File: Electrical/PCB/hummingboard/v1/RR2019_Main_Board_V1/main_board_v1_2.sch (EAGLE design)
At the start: 147 parts, among them CN1 MIRCO_B, IC1 OR_SC70-5, J10 I2C_5V_4, J11 SERVO_LEFT, J12 SERVO_RIGHT, J13 ESC, J14 5V_INPUT, J15 QUAD_ENCODER_2, J16 7.2V_INPUT, J17 I2C_5V_FXIO_1, J18 I2C_5V_FXIO_2, J19 JETSON_TRIGGER, J2 REAR_ENCODER, J20 QUAD_ENCODER_1, J21 BLDC_HALL, J22 SPI_FXIO_1, J3 FRONT_ENCODER, J4 I2C_1V8_1, J5 SPI_2, J6 WIRELESS_MODULE, J7 UART_0, J8 UART_2, J9 STEERING_ANGLE, Q1 BSS138, Q3 DMP2066LSN, Q4 BSS138, Q5 BSS138, Q6 BSS138, Q7 BSS138, Q8 BSS138, U3 ICM-20948, U4 PCA9306

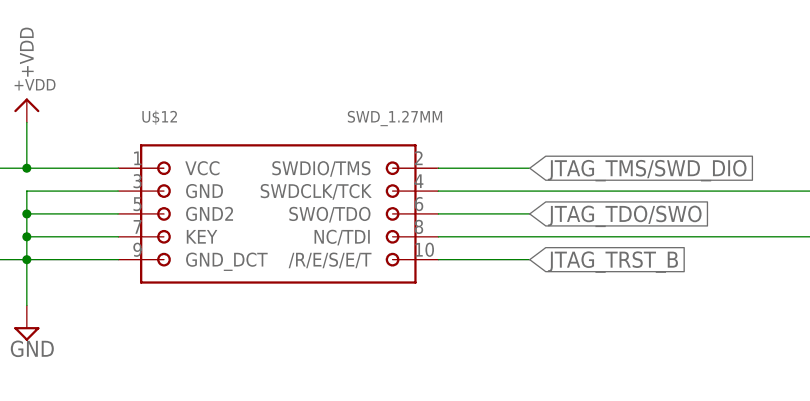
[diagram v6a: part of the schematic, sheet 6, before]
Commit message: silkscreen complete for board
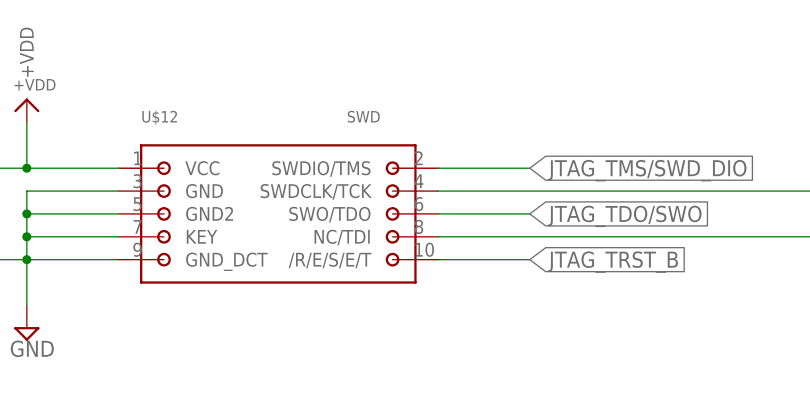
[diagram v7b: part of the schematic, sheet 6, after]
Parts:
- U$12: value SWD_1.27MM -> SWD
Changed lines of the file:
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@@
 <part name="R44" library="RobotRacing2019_Master" deviceset="RES0603" device="" value="10k"/>
 <part name="IC1" library="RobotRacing2019_Master" deviceset="OR_SC70-5" device=""/>
-<part name="U$12" library="RobotRacing2019_Master" deviceset="SWD_1.27MM" device=""/>
+<part name="U$12" library="RobotRacing2019_Master" deviceset="SWD_1.27MM" device="" value="SWD"/>
 <part name="U$18" library="RobotRacing2019_Master" deviceset="+5V" device=""/>
 <part name="U$20" library="RobotRacing2019_Master" deviceset="+3V3" device=""/>

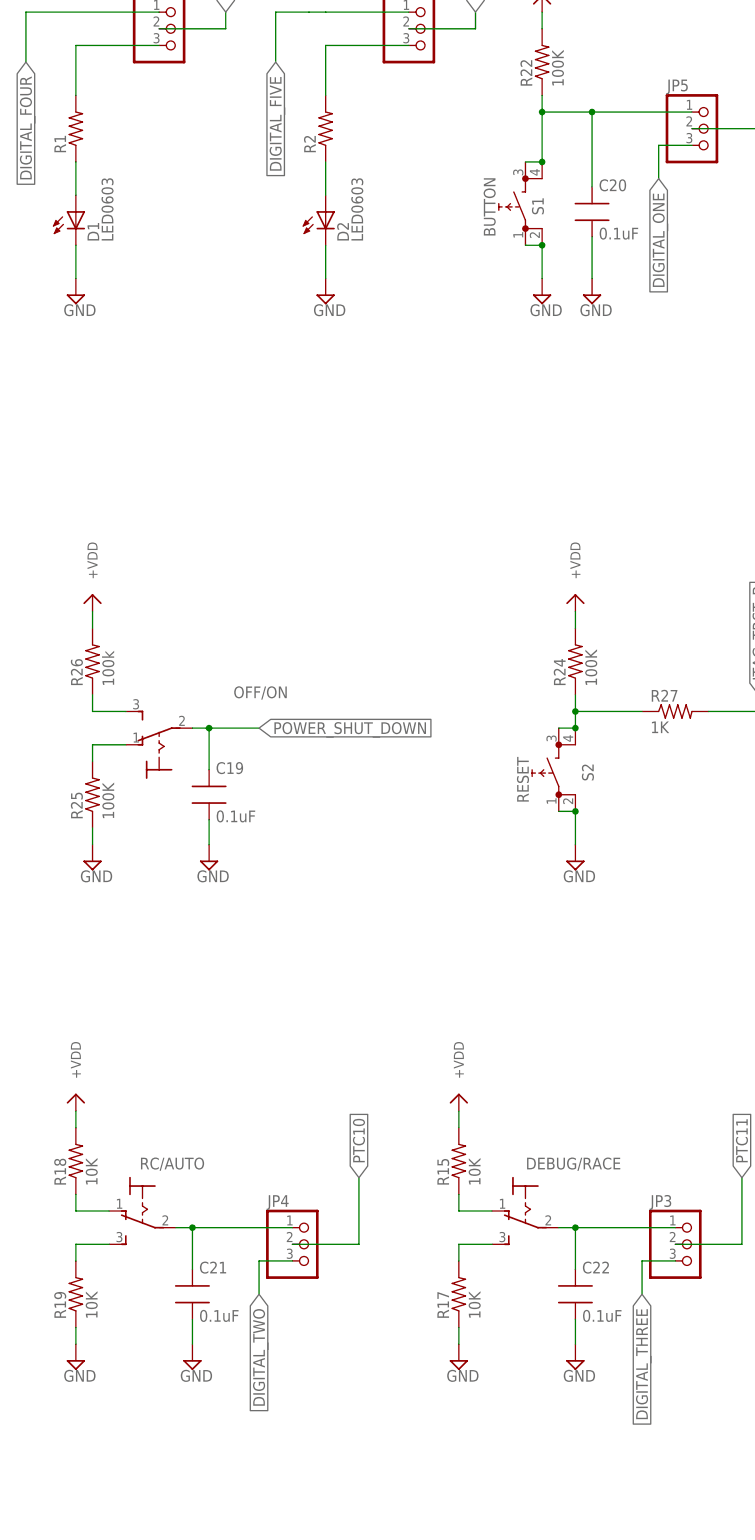
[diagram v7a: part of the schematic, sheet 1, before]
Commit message: change 2 switch to DIP and toggle smaller
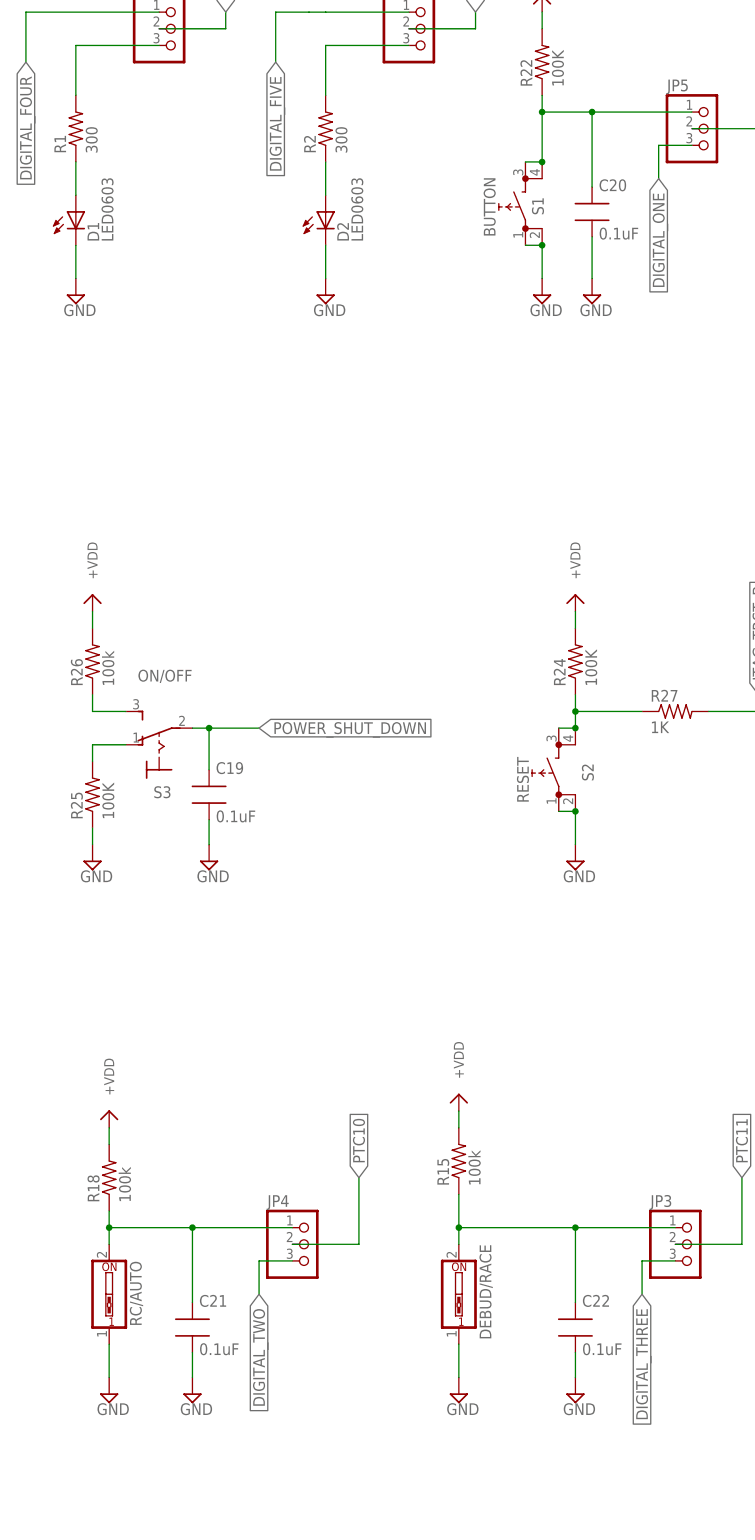
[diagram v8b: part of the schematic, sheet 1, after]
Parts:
- removed D9: LED_GREEN, RobotRacing2019_Master:LED0603
- removed DEBUG/RACE, OFF/ON: (no value), switch:320-916
- removed R17, R19: 10K, RobotRacing2019_Master:RES0603
- removed R45: 150, RobotRacing2019_Master:RES0603
- added DEBUD/RACE: (no value), special:SW_DIP-1
- added S3: ON/OFF, RobotRacing2019_Master:M9040P
- R1, R14, R2: value (none) -> 300
- R12, R13: value 1k -> 300
- R15, R18: value 10K -> 100k
- R16: value (none) -> 120
- R3: value 150 -> 120
- R4: value 150 -> 300
- RC/AUTO: device switch:320-916 -> special:SW_DIP-1
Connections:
- removed net N$28: DEBUG/RACE.S, R17.2
- removed net N$32: R18.1, RC/AUTO.O
- removed net N$33: R19.2, RC/AUTO.S
- removed net N$4: C22.1, DEBUG/RACE.P, JP3.1
- removed net N$42: D9.A, R45.1
- net +1.8V: now also JP6.5; no longer R45.2
- net +3V3: no longer JP6.5
- net GND: now also DEBUD/RACE.1, RC/AUTO.1; no longer D9.C, R17.1, R19.1
- net N$26: now also C22.1, DEBUD/RACE.2, JP3.1; no longer DEBUG/RACE.O
- net N$31: now also R18.1, RC/AUTO.2; no longer RC/AUTO.P
- net N$45: now also S3.S; no longer OFF/ON.S
- net N$46: now also S3.O; no longer OFF/ON.O
- net POWER_SHUT_DOWN: now also S3.P; no longer OFF/ON.P
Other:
- moved on the sheet: C21, C22, R18
